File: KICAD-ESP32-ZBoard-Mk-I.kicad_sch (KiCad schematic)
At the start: 0 parts

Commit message: ADDED most major ICs for DC power, USB-to-UART, and the ESP32 itself.
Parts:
- added C1: 100n, symbol Device:C
- added D1: 1N4004, PCM_Diode_THT_AKL:D_DO-41_SOD81_P7.62mm_Horizontal, symbol PCM_Diode_AKL:1N4004
- added J1: Barrel_Jack_MountingPin, Connector_BarrelJack:BarrelJack_Horizontal, symbol Connector:Barrel_Jack_MountingPin
- added J2: USB_A, symbol Connector:USB_A
- added U1: ESP32-WROOM-32UE, RF_Module:ESP32-WROOM-32UE, symbol ZCustomSymbols:ESP32-WROOM-32UE
- added U2: SY8120IABC, Package_TO_SOT_SMD:SOT-23-6, symbol ZCustomSymbols:SY8120IABC
- added U3: CH340C, Package_SO:SOIC-16_3.9x9.9mm_P1.27mm, symbol Interface_USB:CH340C
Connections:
- new net +3V3: C1.1, U1.2 (VIN), U3.16 (VCC), U3.4 (V3)
- new net D+: J2.3 (D+), U3.5 (UD+)
- new net D-: J2.2 (D-), U3.6 (UD-)
- new net GND: C1.2, J2.4 (GND), J2.5 (Shield), U1.1 (GND), U1.15 (GND), U1.38 (GND), U1.39 (GND), U3.1 (GND)
- new net RX_UART_ESP32: U1.34 (RXD0/IO3), U3.2 (TXD)
- new net TX_UART_ESP32: U1.35 (TXD0/IO1), U3.3 (RXD)
- no-connect marks 0 -> 2
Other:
- note added: "TODO auto bootmode flash logic"
- note added: "TODO map header pins for GPIOs"
- note added: "TODO power supply TODO add low-current (so I don't get blinded!!!) LED TODO power rail pins (jmpr conn w/ header pins)"
- company: (none) -> The Zachary of Hobbs
- title: (none) -> ZBoard Mk-I

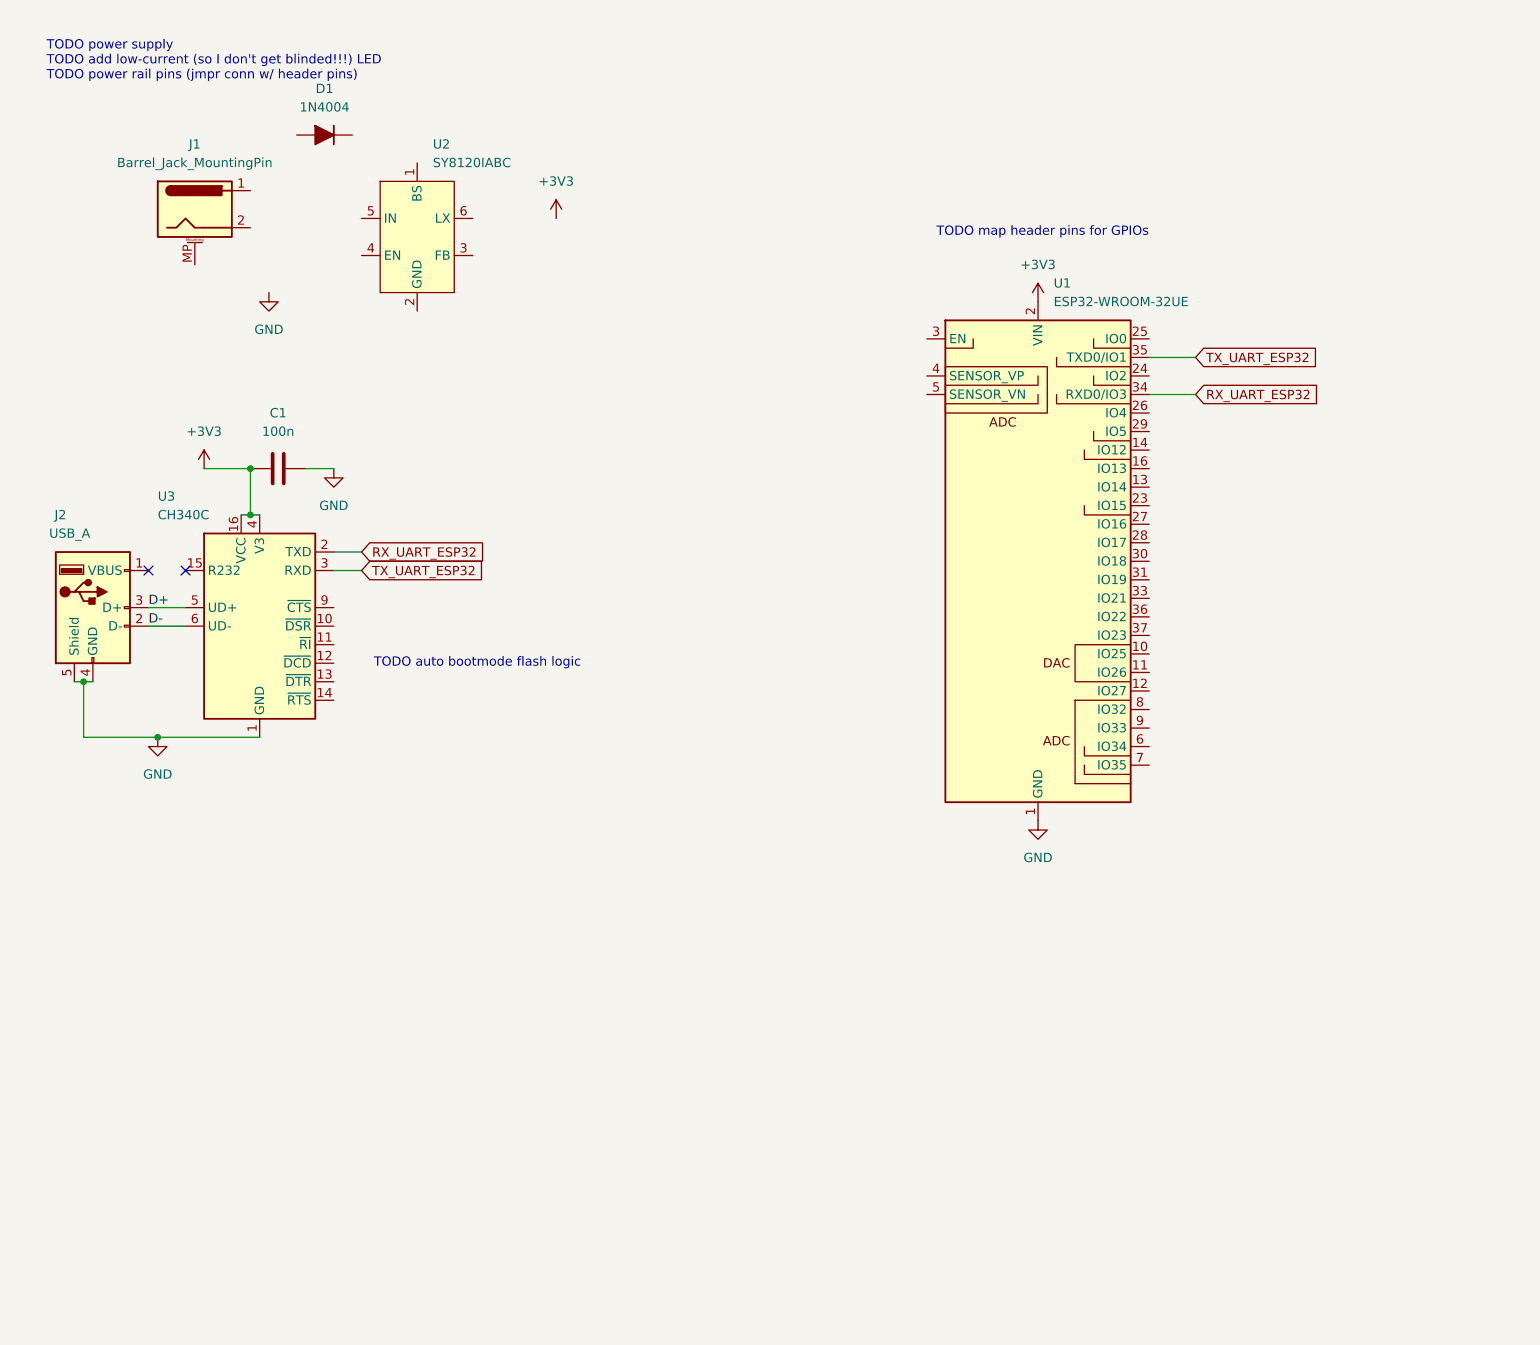
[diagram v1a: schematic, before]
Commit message: ADDED power supply. ADDED indicator LED.
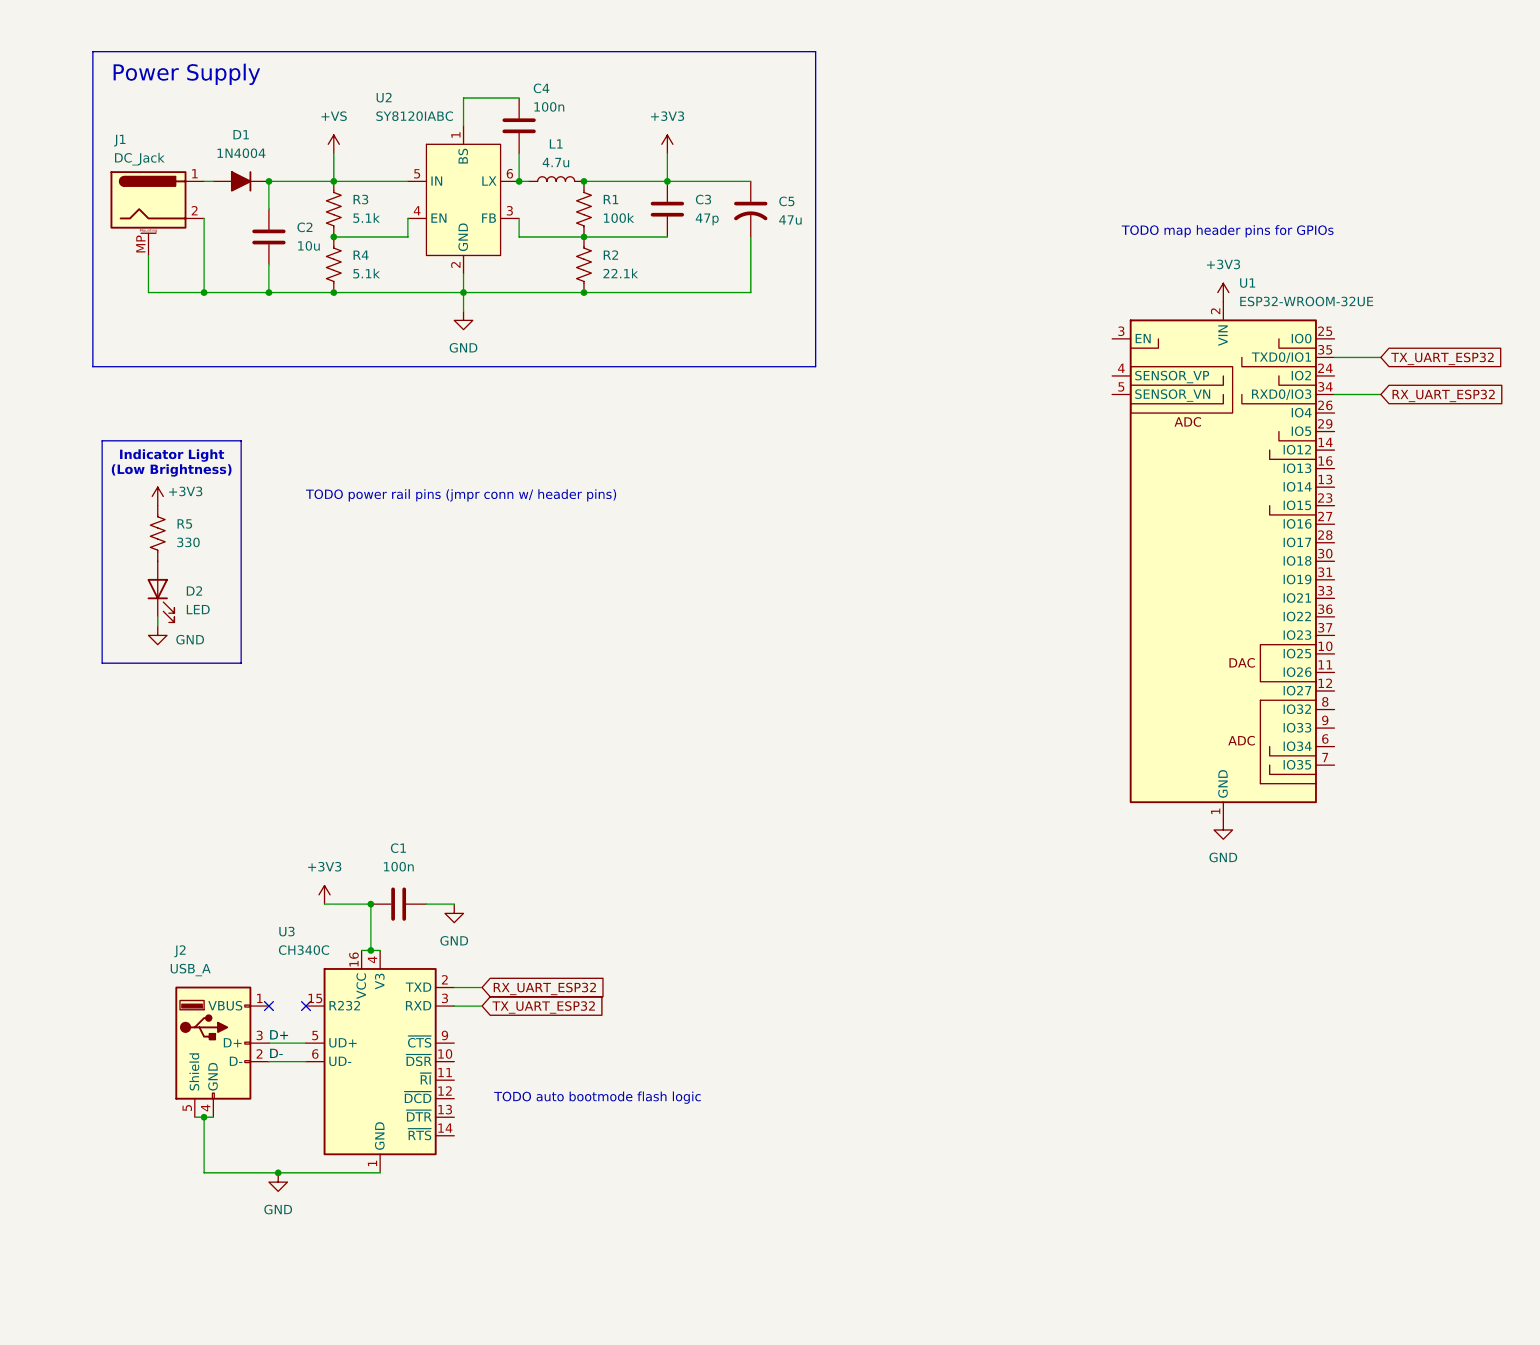
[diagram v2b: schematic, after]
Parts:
- added C2: 10u, symbol Device:C
- added C3: 47p, symbol Device:C
- added C4: 100n, symbol Device:C
- added C5: 47u, symbol Device:C_US
- added D2: LED, symbol Device:LED
- added L1: 4.7u, symbol Device:L
- added R1: 100k, symbol Device:R_US
- added R2: 22.1k, symbol Device:R_US
- added R3, R4: 5.1k, symbol Device:R_US
- added R5: 330, symbol Device:R_US
- J1: value Barrel_Jack_MountingPin -> DC_Jack
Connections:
- net +3V3: now also C3.1, C5.1, L1.2, R1.2, R5.1
- net GND: now also J1.2, J1.MP (MountPin), U2.2 (GND), C2.2, C5.2, D2.1 (K), R2.2, R4.2
- net at U2.1 (BS): now also C4.1
- net at U2.3 (FB): now also C3.2, R1.1, R2.1
- net at U2.4 (EN): now also R3.2, R4.1
- net +VS: now reaches U2.5 (IN)
- net +VS: now also D1.1 (K), C2.1, R3.1
- net at U2.6 (LX): now also C4.2, L1.1
- net at J1.1: now also D1.2 (A)
- new net: D2.2 (A), R5.2
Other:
- note added: "Indicator Light (Low Brightness)"
- note added: "Power Supply"
- note added: "TODO power rail pins (jmpr conn w/ header pins)"
- note removed: "TODO power supply TODO add low-current (so I don't get blinded!!!) LED TODO power rail pins (jmpr conn w/ header pins)"
- moved on the sheet: C1, D1, J1, J2, U1, U2, U3

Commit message: ADDED boot mode control logic. ADDED power-rail selection pin headers.
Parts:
- added J3: Conn_01x02_Pin-RAIL_1, Connector_PinHeader_2.54mm:PinHeader_1x02_P2.54mm_Vertical, symbol Connector:Conn_01x02_Pin
- added J4: Conn_01x02_Pin-RAIL_2, Connector_PinHeader_2.54mm:PinHeader_1x02_P2.54mm_Vertical, symbol Connector:Conn_01x02_Pin
- added J5: Conn_01x02_Pin-RAIL_3, Connector_PinHeader_2.54mm:PinHeader_1x02_P2.54mm_Vertical, symbol Connector:Conn_01x02_Pin
- added J6: Conn_01x03_Pin-RAIL_1, Connector_PinHeader_2.54mm:PinHeader_1x03_P2.54mm_Vertical, symbol Connector:Conn_01x03_Pin
- added J7: Conn_01x03_Pin-RAIL_2, Connector_PinHeader_2.54mm:PinHeader_1x03_P2.54mm_Vertical, symbol Connector:Conn_01x03_Pin
- added J8: Conn_01x03_Pin-RAIL_3, Connector_PinHeader_2.54mm:PinHeader_1x03_P2.54mm_Vertical, symbol Connector:Conn_01x03_Pin
- added U4: 74HCT00, symbol 74xx:74HCT00
- D2: LCSC Part # (none) -> C497928
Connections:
- net +3V3: now also J6.1 (Pin_1), J7.1 (Pin_1), J8.1 (Pin_1), U4.14 (VCC)
- net +VS: now also J6.3 (Pin_3), J7.3 (Pin_3), J8.3 (Pin_3)
- net GND: now also J3.2 (Pin_2), J4.2 (Pin_2), J5.2 (Pin_2), U4.7 (GND)
- net IO0: now reaches U1.25 (IO0)
- net IO0: now also U4.6
- net EN: now reaches U1.3 (EN)
- net EN: now also U4.8
- net DTR: now reaches U3.13 (~{DTR})
- net DTR: now also U4.1, U4.2, U4.9
- net RTS: now reaches U3.14 (~{RTS})
- net RTS: now also U4.12, U4.13, U4.5
- new net: U4.10, U4.11
- new net: J4.1 (Pin_1), J7.2 (Pin_2)
- new net: J5.1 (Pin_1), J8.2 (Pin_2)
- new net: J3.1 (Pin_1), J6.2 (Pin_2)
- new net: U4.3, U4.4
- no-connect marks 2 -> 6
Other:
- note added: "Bootmode Logic"
- note added: "Header pin jumper caps connect pins"
- note added: "Power-Rail Pins"
- note added: "USB Serial-UART Interface"
- note removed: "TODO auto bootmode flash logic"
- note removed: "TODO power rail pins (jmpr conn w/ header pins)"
- moved on the sheet: C1, J2, U3
